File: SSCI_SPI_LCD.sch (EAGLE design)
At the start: 33 parts, among them IC3 74LVC541_RGY, X1 PHA-1X08SG, X2 PHA-1X08SG

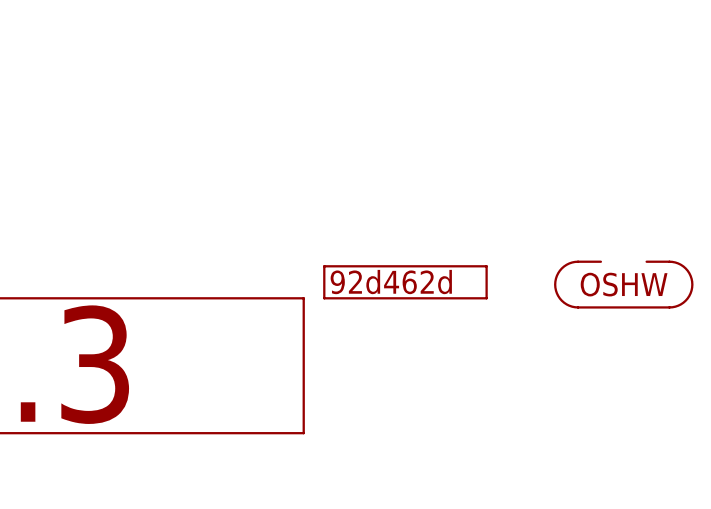
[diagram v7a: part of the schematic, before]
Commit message: [ BRD ] add C5 ground via; git revision update
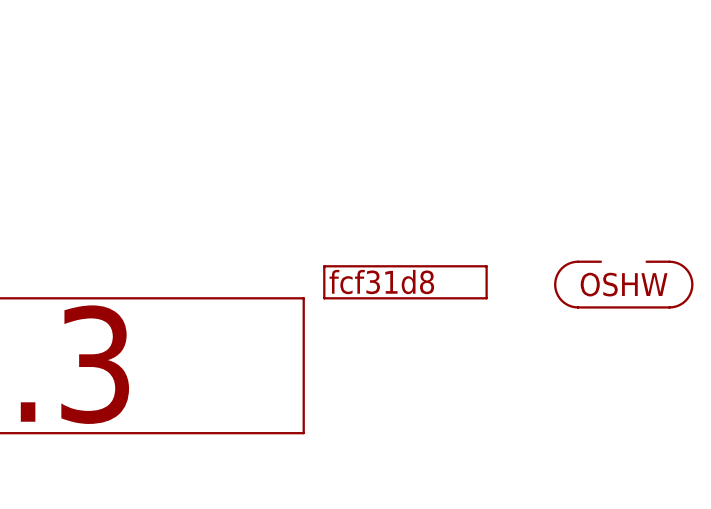
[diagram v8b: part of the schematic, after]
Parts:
- GIT1: value 92d462d -> fcf31d8
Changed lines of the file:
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@@
 <part name="P3" library="mylib" deviceset="PCB_CORNER" device=""/>
 <part name="P4" library="mylib" deviceset="PCB_CORNER" device=""/>
-<part name="GIT1" library="git-revision" deviceset="GIT-REVISION" device="_1.2" value="92d462d"/>
+<part name="GIT1" library="git-revision" deviceset="GIT-REVISION" device="_1.2" value="fcf31d8"/>
 <part name="FRAME1" library="frames" deviceset="A4L-LOC" device=""/>
 <part name="ICON1" library="mylib" deviceset="ICON_REVISION" device="_1.7" value="r0.3"/>
